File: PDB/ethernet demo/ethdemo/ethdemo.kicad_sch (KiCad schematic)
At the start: 56 parts, among them J1 0826-1X1T-GJ-F, J2 0826-1X1T-GJ-F, Q1 CSD19538Q3AT, U1 STM32H742VGTx, U2 KSZ8863RLLI, U3 TPS23861PWR

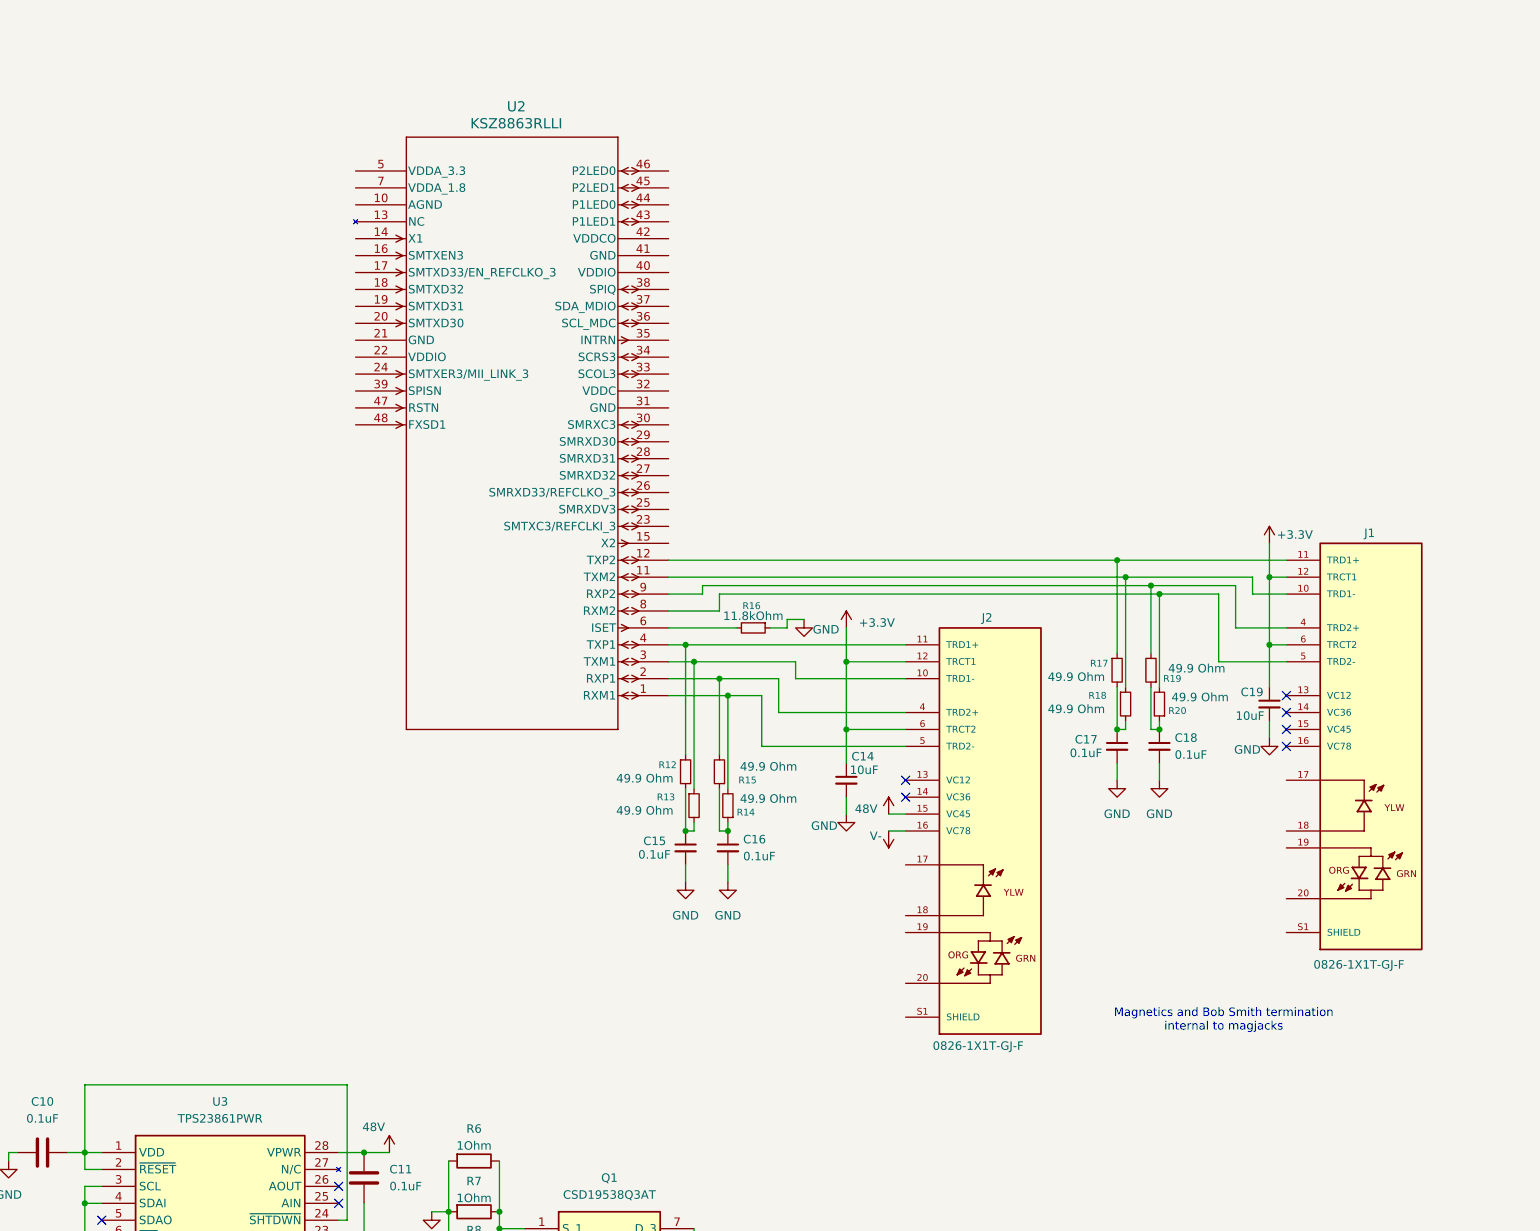
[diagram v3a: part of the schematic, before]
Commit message: Flesh out switch schematic
Added power and RMLL interface to switch with blank resistors for optional use of RMLL and I2C to the MCU
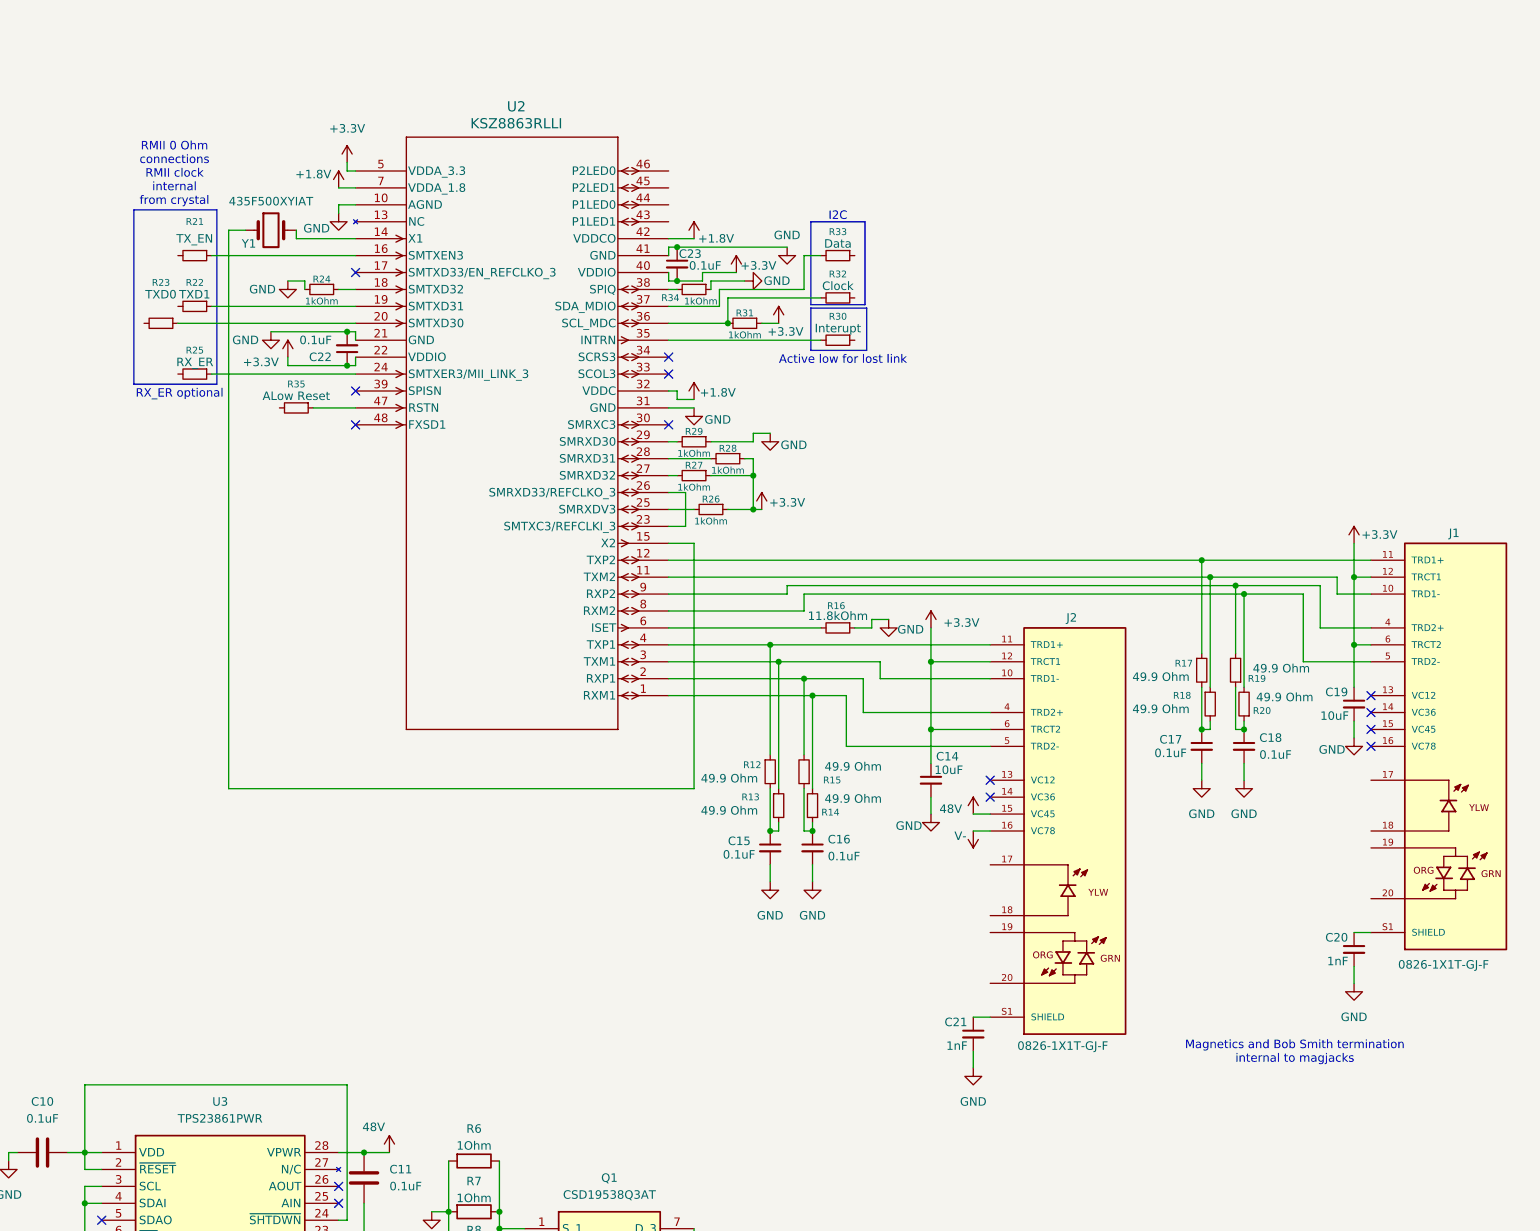
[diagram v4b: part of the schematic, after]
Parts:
- added C20, C21: 1nF, symbol Device:C_Small
- added C22, C23: 0.1uF, symbol Device:C_Small
- added R21: TX_EN, symbol Device:R_Small
- added R22: TXD1, symbol Device:R_Small
- added R23: TXD0, symbol Device:R_Small
- added R24, R26, R27, R28, R29, R31, R34: 1kOhm, symbol Device:R_Small
- added R25: RX_ER, symbol Device:R_Small
- added R30: Interupt, symbol Device:R_Small
- added R32: Clock, symbol Device:R_Small
- added R33: Data, symbol Device:R_Small
- added R35: ALow Reset, symbol Device:R_Small
- added Y1: 435F500XYIAT, Crystal:Crystal_SMD_5032-2Pin_5.0x3.2mm, symbol Device:Crystal
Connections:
- net +3.3V: now also U2.22 (VDDIO), U2.40 (VDDIO), U2.5 (VDDA_3.3), C22.1, C23.2, R26.1, R27.1, R28.1, R31.1
- net GND: now also U2.10 (AGND), U2.21 (GND), U2.31 (GND), U2.41 (GND), C20.2, C21.2, C22.2, C23.1, R24.2, R29.1, R34.1
- net at J1.S1 (SHIELD), J1.S2 (SHIELD): now also C20.1
- net at J2.S1 (SHIELD), J2.S2 (SHIELD): now also C21.1
- net at U2.14 (X1): now also Y1.2
- net at U2.15 (X2): now also Y1.1
- net at U2.16 (SMTXEN3): now also R21.1
- net at U2.18 (SMTXD32): now also R24.1
- net at U2.19 (SMTXD31): now also R22.1
- net at U2.20 (SMTXD30): now also R23.1
- net at U2.23 (SMTXC3/REFCLKI_3): now also U2.26 (SMRXD33/REFCLKO_3)
- net at U2.24 (SMTXER3/MII_LINK_3): now also R25.1
- net at U2.25 (SMRXDV3): now also R26.2
- net at U2.27 (SMRXD32): now also R27.2
- net at U2.28 (SMRXD31): now also R28.2
- net at U2.29 (SMRXD30): now also R29.2
- net +1.8V: now reaches U2.32 (VDDC)
- net +1.8V: now also U2.42 (VDDCO), U2.7 (VDDA_1.8)
- net at U2.35 (INTRN): now also R30.2
- net at U2.36 (SCL_MDC): now also R31.2, R32.2
- net at U2.37 (SDA_MDIO): now also R33.2
- net at U2.38 (SPIQ): now also R34.2
- net at U2.47 (RSTN): now also R35.1
- no-connect marks 57 -> 63
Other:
- note added: "Active low for lost link"
- note added: "I2C"
- note added: "RMII 0 Ohm connections RMII clock internal from crystal"
- note added: "RX_ER optional"
- moved on the sheet: C14, C15, C16, C17, C18, C19, J1, J2, R12, R13, R14, R15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

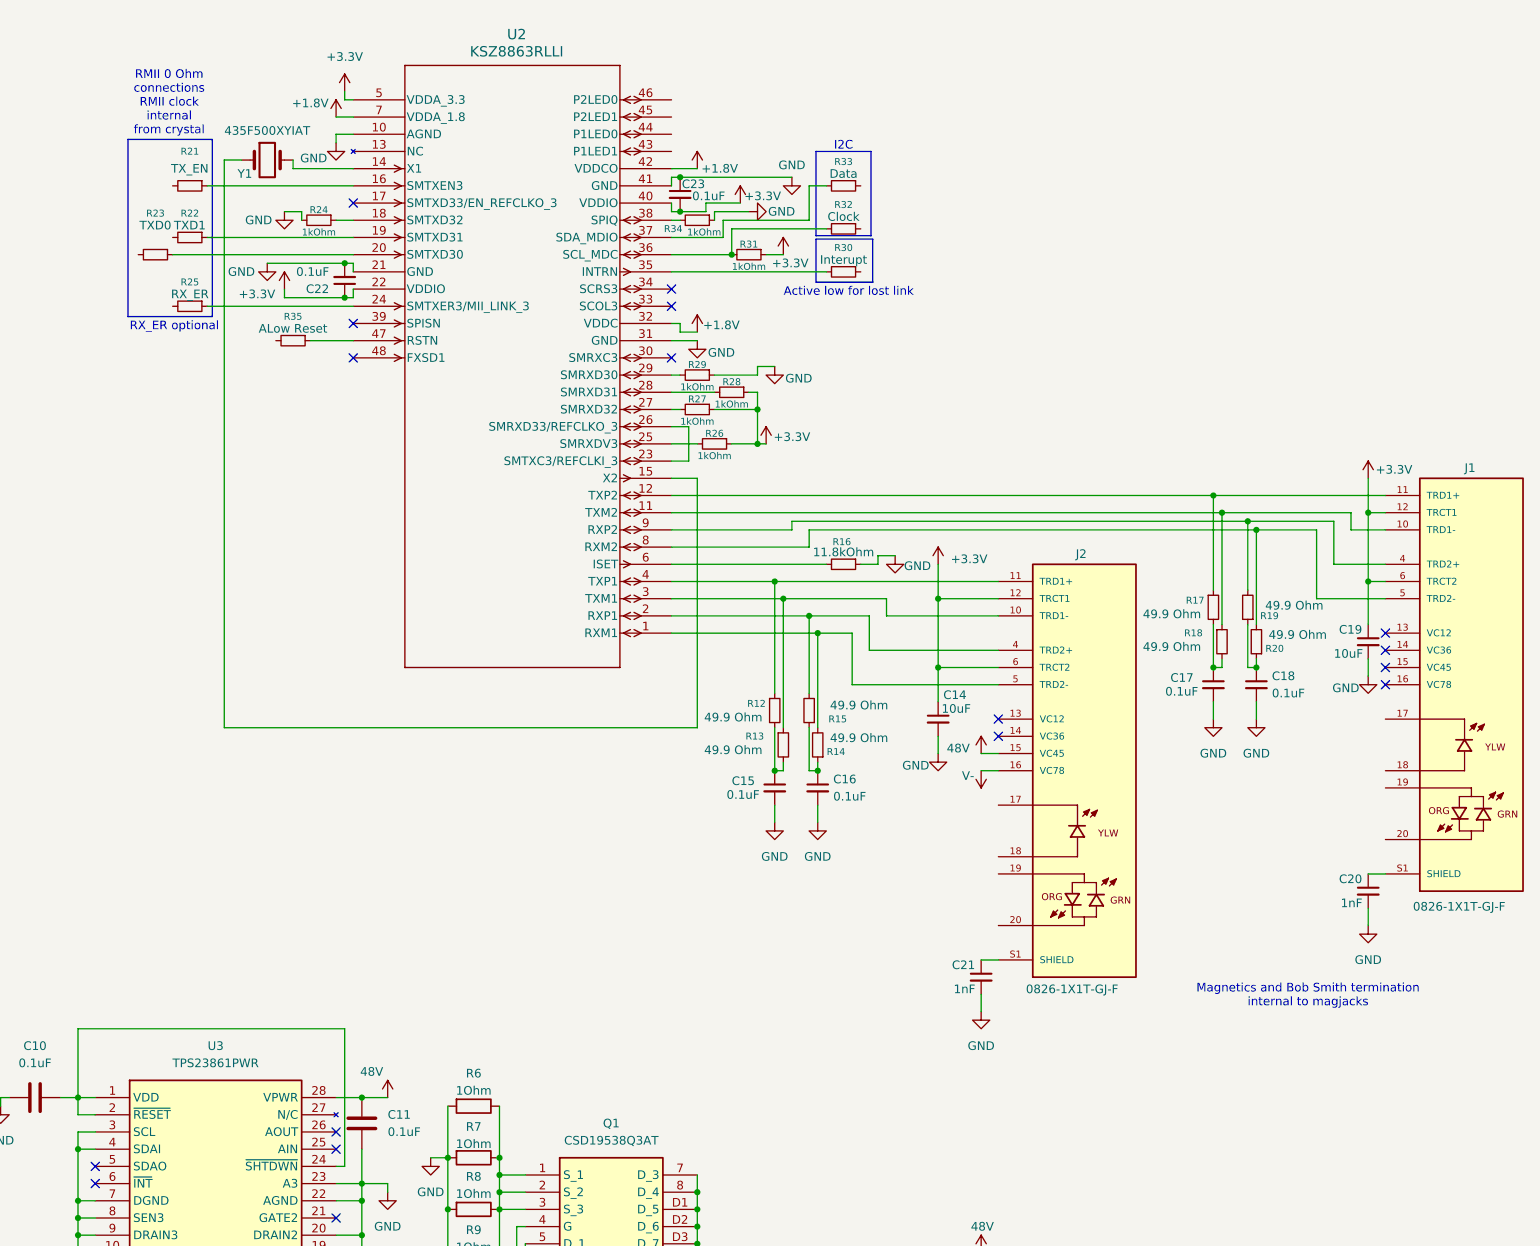
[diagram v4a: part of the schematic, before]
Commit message: repaired a portion of the switch circuit
Discovered that some of the switch is designed for MLL not RMLL and started fixing it
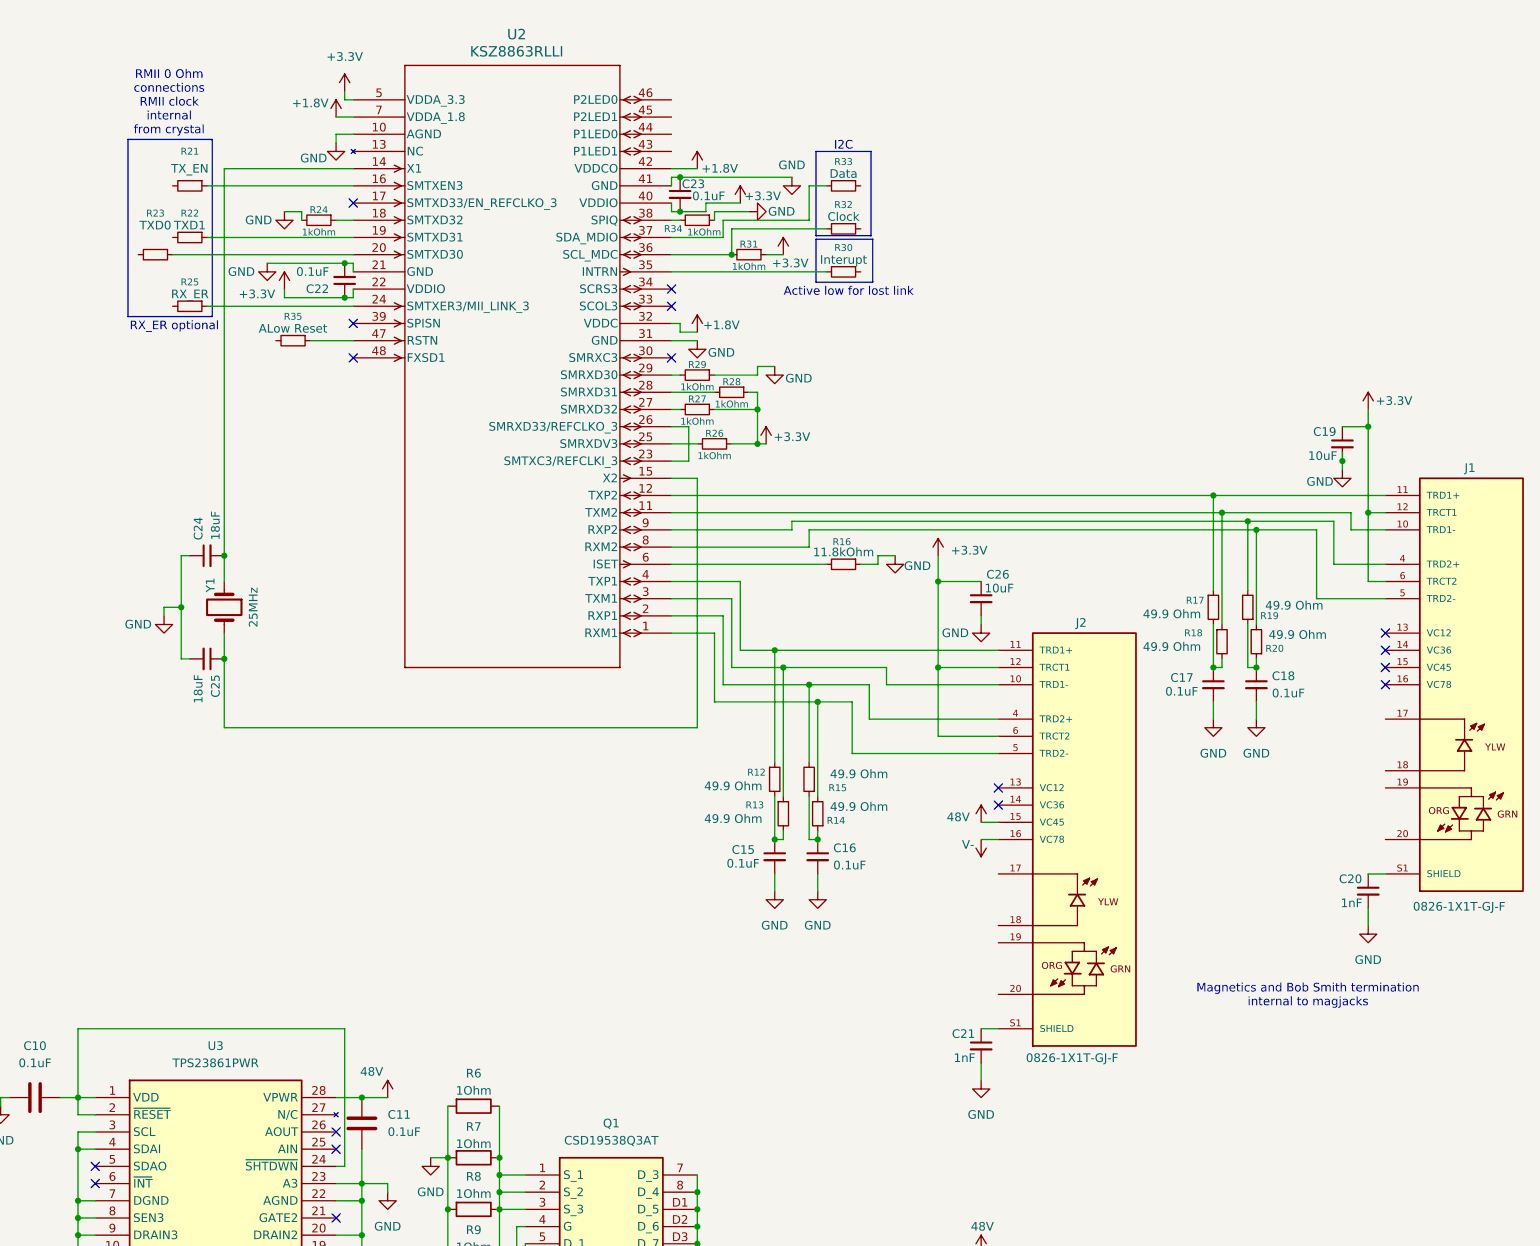
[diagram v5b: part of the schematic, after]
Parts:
- removed C14: 10uF, symbol Device:C_Small
- added C24, C25: 18uF, symbol Device:C_Small
- added C26: 10uF, symbol Device:C_Small
- Y1: value 435F500XYIAT -> 25MHz
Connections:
- net +3.3V: now also C26.1
- net GND: now also C24.1, C25.2, C26.2
- net at Y1.2: now also U2.15 (X2), C25.1; no longer U2.14 (X1)
- net at Y1.1: now also U2.14 (X1), C24.2; no longer U2.15 (X2)
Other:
- moved on the sheet: C15, C16, C19, C21, J2, R12, R13, R14, R15, Y1
